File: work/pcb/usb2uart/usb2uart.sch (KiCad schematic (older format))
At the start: 12 parts, among them J1 USB, J2 HEADER, U1 CP2104

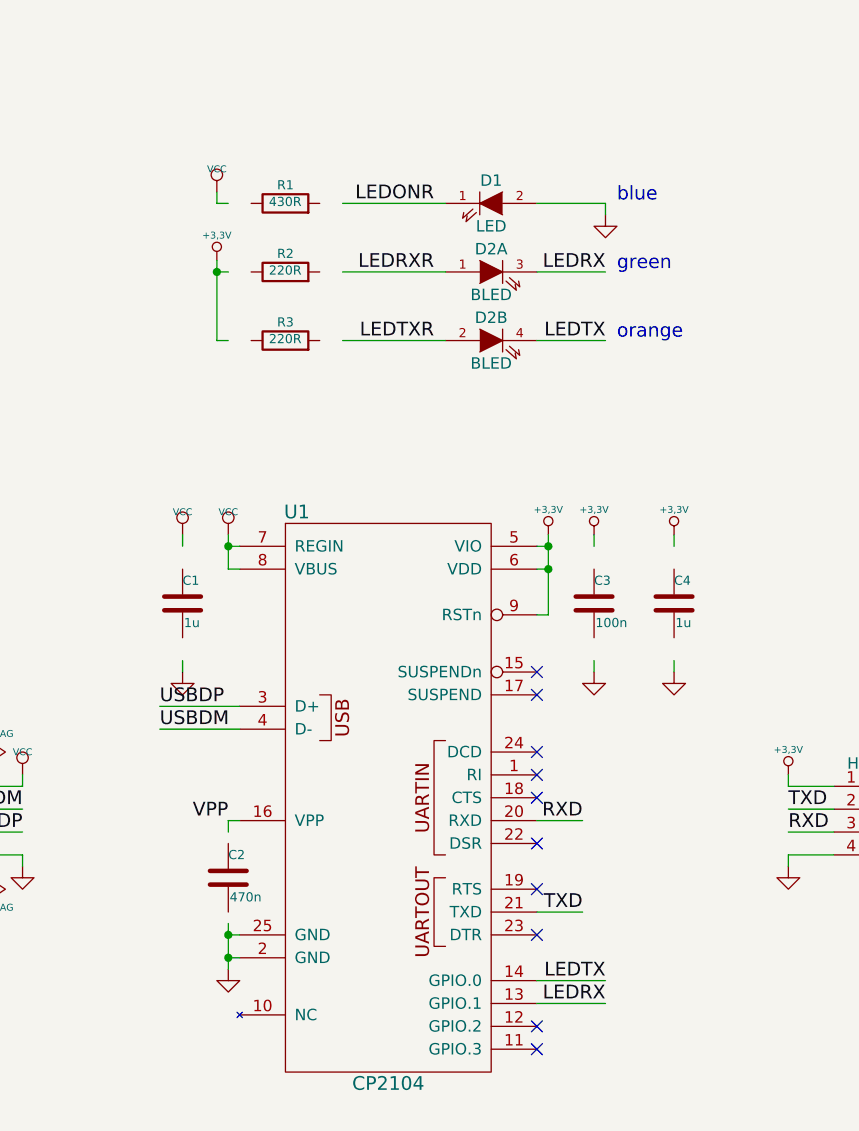
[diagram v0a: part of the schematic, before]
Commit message: [pcb] πρώτη ολοκληρωμένη έκδοση κυκλώματος, μαζί με αρχεία παραγωγής
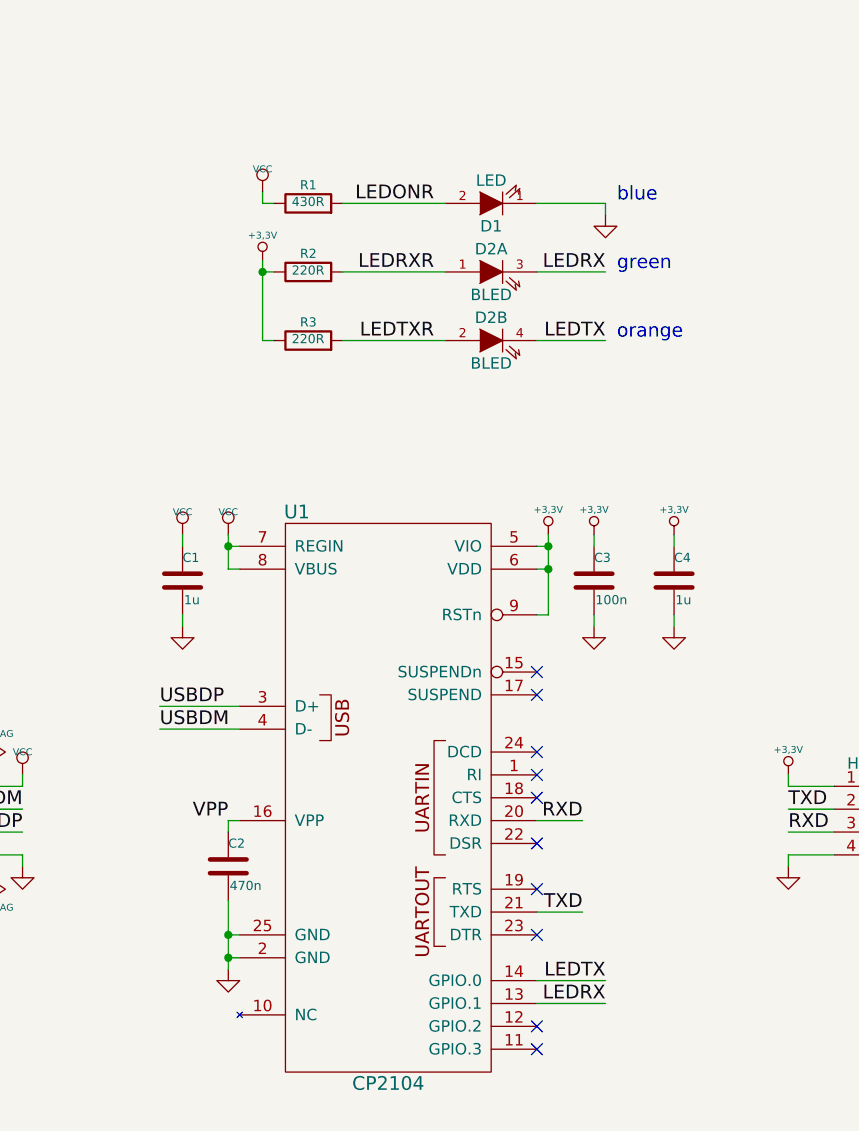
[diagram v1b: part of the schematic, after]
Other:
- moved on the sheet: C1, C2, C3, C4, R1, R2, R3
